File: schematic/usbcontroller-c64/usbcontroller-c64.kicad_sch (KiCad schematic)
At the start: 14 parts, among them J1 Conn_01x20_Socket, J2 Conn_01x20_Socket, J3 Conn_01x06_Socket, J4 Conn_01x02_Socket, Q1 PN2222A, Q2 PN2222A, Q3 PN2222A, Q4 PN2222A, Q5 PN2222A

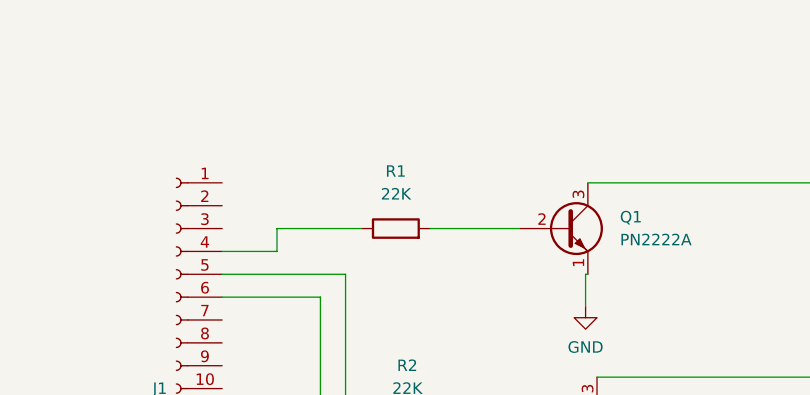
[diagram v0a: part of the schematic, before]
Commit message: add tx/rx for debug
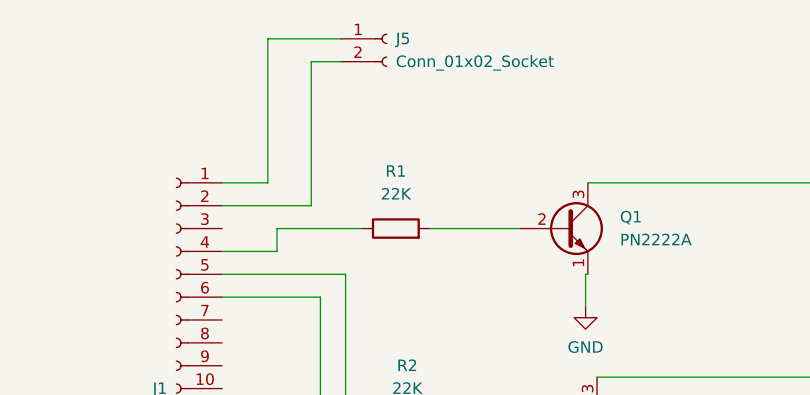
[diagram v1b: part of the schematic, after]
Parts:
- added J5: Conn_01x02_Socket, Connector_PinSocket_2.54mm:PinSocket_1x02_P2.54mm_Vertical, symbol Connector:Conn_01x02_Socket
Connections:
- net at J1.1 (Pin_1): now also J5.1 (Pin_1)
- net at J1.2 (Pin_2): now also J5.2 (Pin_2)
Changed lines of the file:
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@@
+    (stroke (width 0) (type default))
+  )
+  (wire (pts (xy 104.14 44.958) (xy 107.442 44.958))
     (stroke (width 0) (type default))
   )
@@
     (stroke (width 0) (type default))
   )
+  (wire (pts (xy 99.314 42.418) (xy 107.442 42.418))
+    (stroke (width 0) (type default))
+  )
   (wire (pts (xy 109.22 128.27) (xy 114.3 128.27))
     (stroke (width 0) (type default))
@@
     (stroke (width 0) (type default))
   )
+  (wire (pts (xy 99.314 58.42) (xy 99.314 42.418))
+    (stroke (width 0) (type default))
+  )
   (wire (pts (xy 67.564 122.936) (xy 109.22 122.936))
     (stroke (width 0) (type default))
   )
+  (wire (pts (xy 94.234 60.96) (xy 104.14 60.96))
+    (stroke (width 0) (type default))
+  )
   (wire (pts (xy 176.784 148.59) (xy 176.784 104.14))
     (stroke (width 0) (type default))
   )
+  (wire (pts (xy 94.234 58.42) (xy 99.314 58.42))
+    (stroke (width 0) (type default))
+  )
   (wire (pts (xy 138.176 132.334) (xy 138.176 137.414))
+    (stroke (width 0) (type default))
+  )
+  (wire (pts (xy 104.14 60.96) (xy 104.14 44.958))
     (stroke (width 0) (type default))
   )
@@
         )
       )
+    )
+  )
+  (symbol (lib_id "Connector:Conn_01x02_Socket") (at 112.522 42.418 0) (unit 1)
+    (in_bom yes) (on_board yes) (dnp no) (fields_autoplaced)
+    (property "Reference" "J5" (at 113.538 42.418 0)
+      (effects (font (size 1.27 1.27)) (justify left))
+    )
+    (property "Value" "Conn_01x02_Socket" (at 113.538 44.958 0)
+      (effects (font (size 1.27 1.27)) (justify left))
+    )
+    (property "Footprint" "Connector_PinSocket_2.54mm:PinSocket_1x02_P2.54mm_Vertical" (at 112.522 42.418 0)
+      (effects (font (size 1.27 1.27)) hide)
+    )
+    (property "Datasheet" "~" (at 112.522 42.418 0)
+      (effects (font (size 1.27 1.27)) hide)
+    )
+    (pin "1")
+    (pin "2")
+    (instances
+      (project "usbcontroller-c64"
+        (path "/8450b7a4-7acf-420a-93b2-b80915645b62"
+          (reference "J5") (unit 1)
+        )
+      )

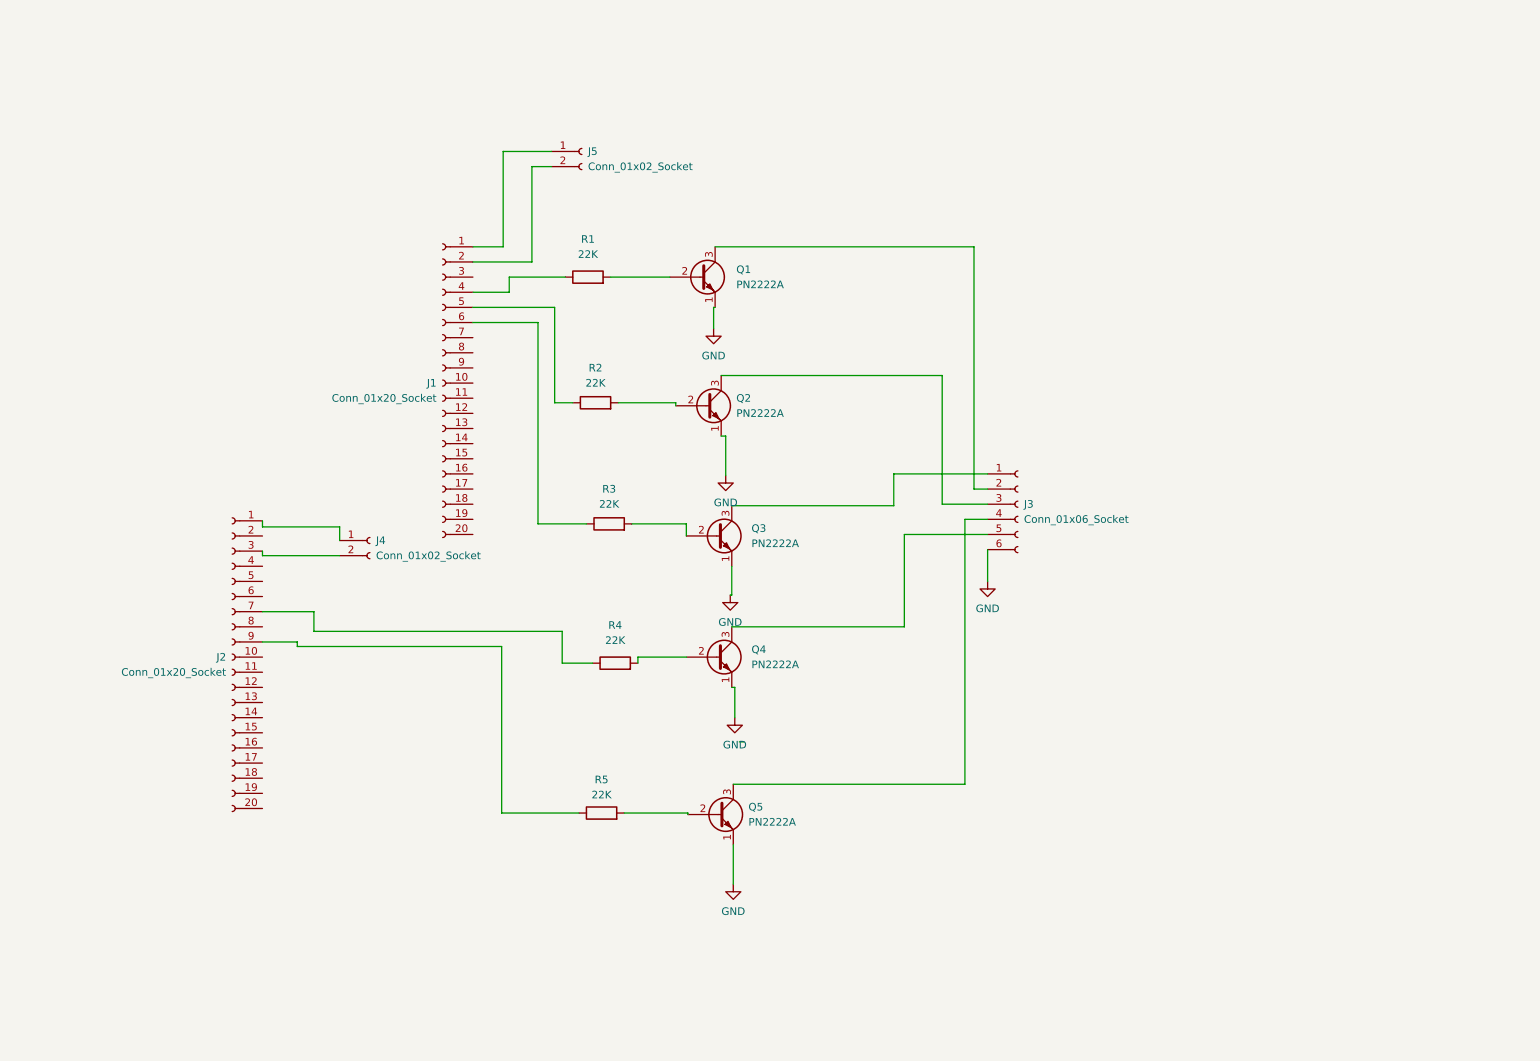
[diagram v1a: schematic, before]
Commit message: update schematic to usb db9 connector and power
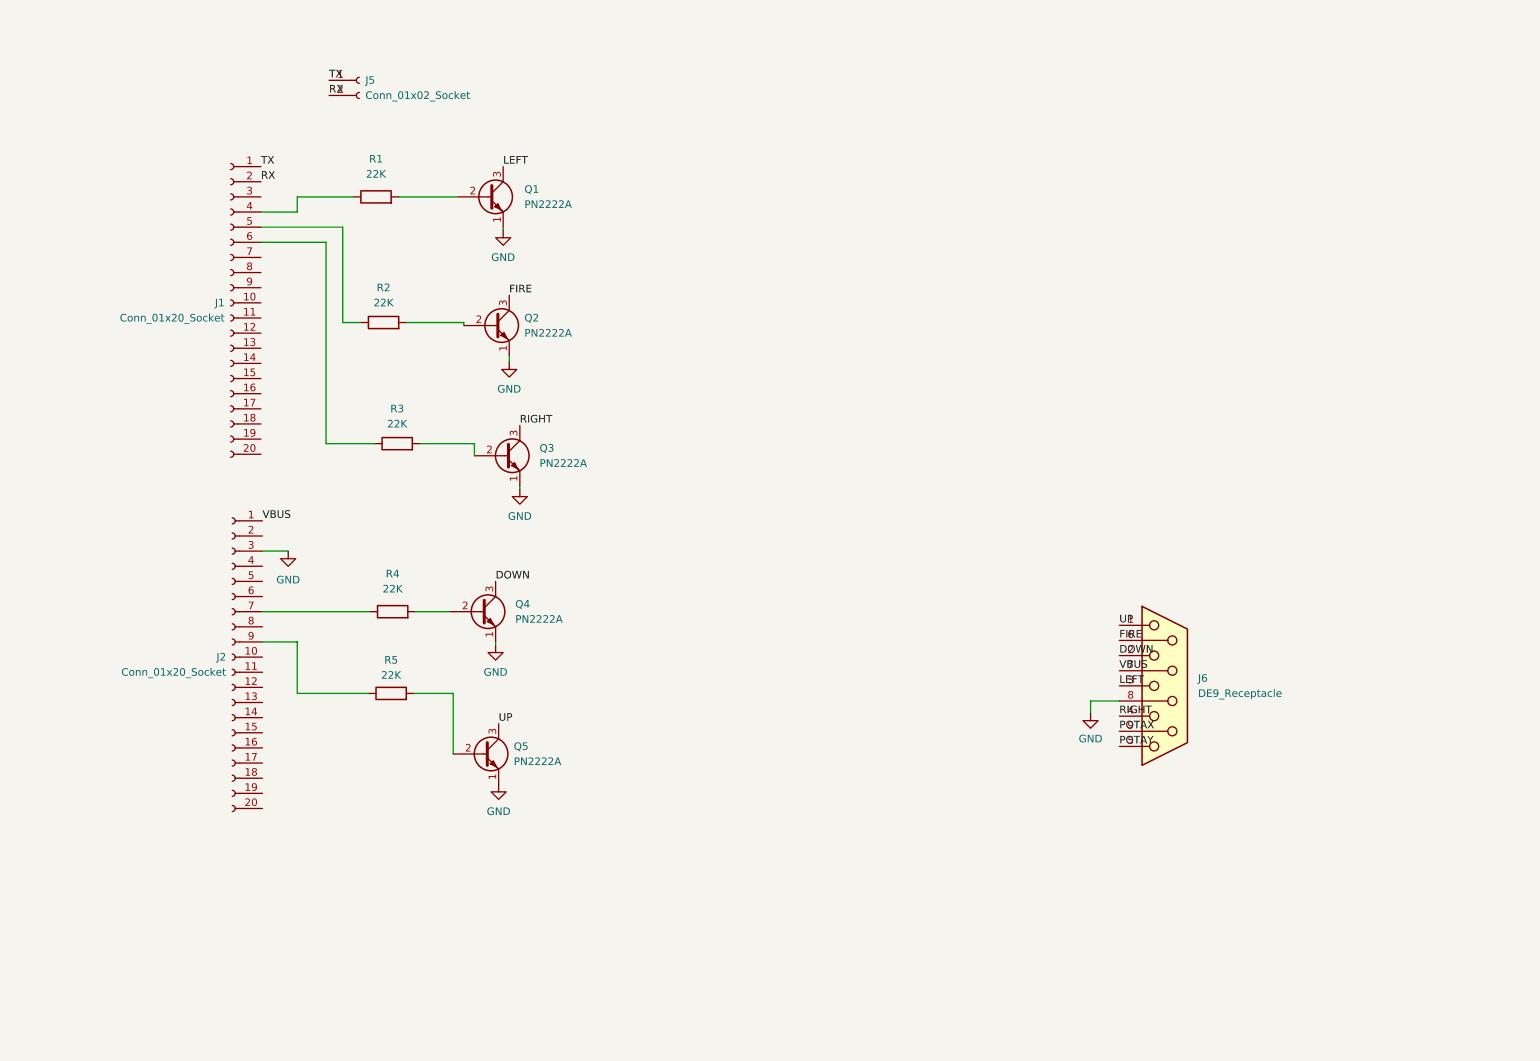
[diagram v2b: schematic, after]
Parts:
- removed J3: Conn_01x06_Socket, Connector_PinSocket_2.54mm:PinSocket_1x06_P2.54mm_Vertical, symbol Connector:Conn_01x06_Socket
- removed J4: Conn_01x02_Socket, Connector_PinSocket_2.54mm:PinSocket_1x02_P2.54mm_Vertical, symbol Connector:Conn_01x02_Socket
- added J6: DE9_Receptacle, Connector_Dsub:DSUB-9_Female_Horizontal_P2.77x2.84mm_EdgePinOffset7.70mm_Housed_MountingHolesOffset9.12mm, symbol Connector:DE9_Receptacle
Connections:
- net GND: now also J2.3 (Pin_3), J6.8
- net FIRE: now reaches Q2.3 (C)
- net FIRE: now also J6.6
- net UP: now reaches Q5.3 (C)
- net UP: now also J6.1
- net TX: now reaches J1.1 (Pin_1), J5.1 (Pin_1)
- net RX: now reaches J1.2 (Pin_2), J5.2 (Pin_2)
- net LEFT: now reaches Q1.3 (C)
- net LEFT: now also J6.3
- net RIGHT: now reaches Q3.3 (C)
- net RIGHT: now also J6.4
- net DOWN: now reaches Q4.3 (C)
- net DOWN: now also J6.2
- net VBUS: now reaches J2.1 (Pin_1)
- net VBUS: now also J6.7
- new net POTAX: J6.9
- new net POTAY: J6.5
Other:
- moved on the sheet: J1, J5, Q1, Q2, Q3, Q4, Q5, R1, R2, R3, R4, R5

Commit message: remove forked pico-sdk depeancy and get back on the normal one
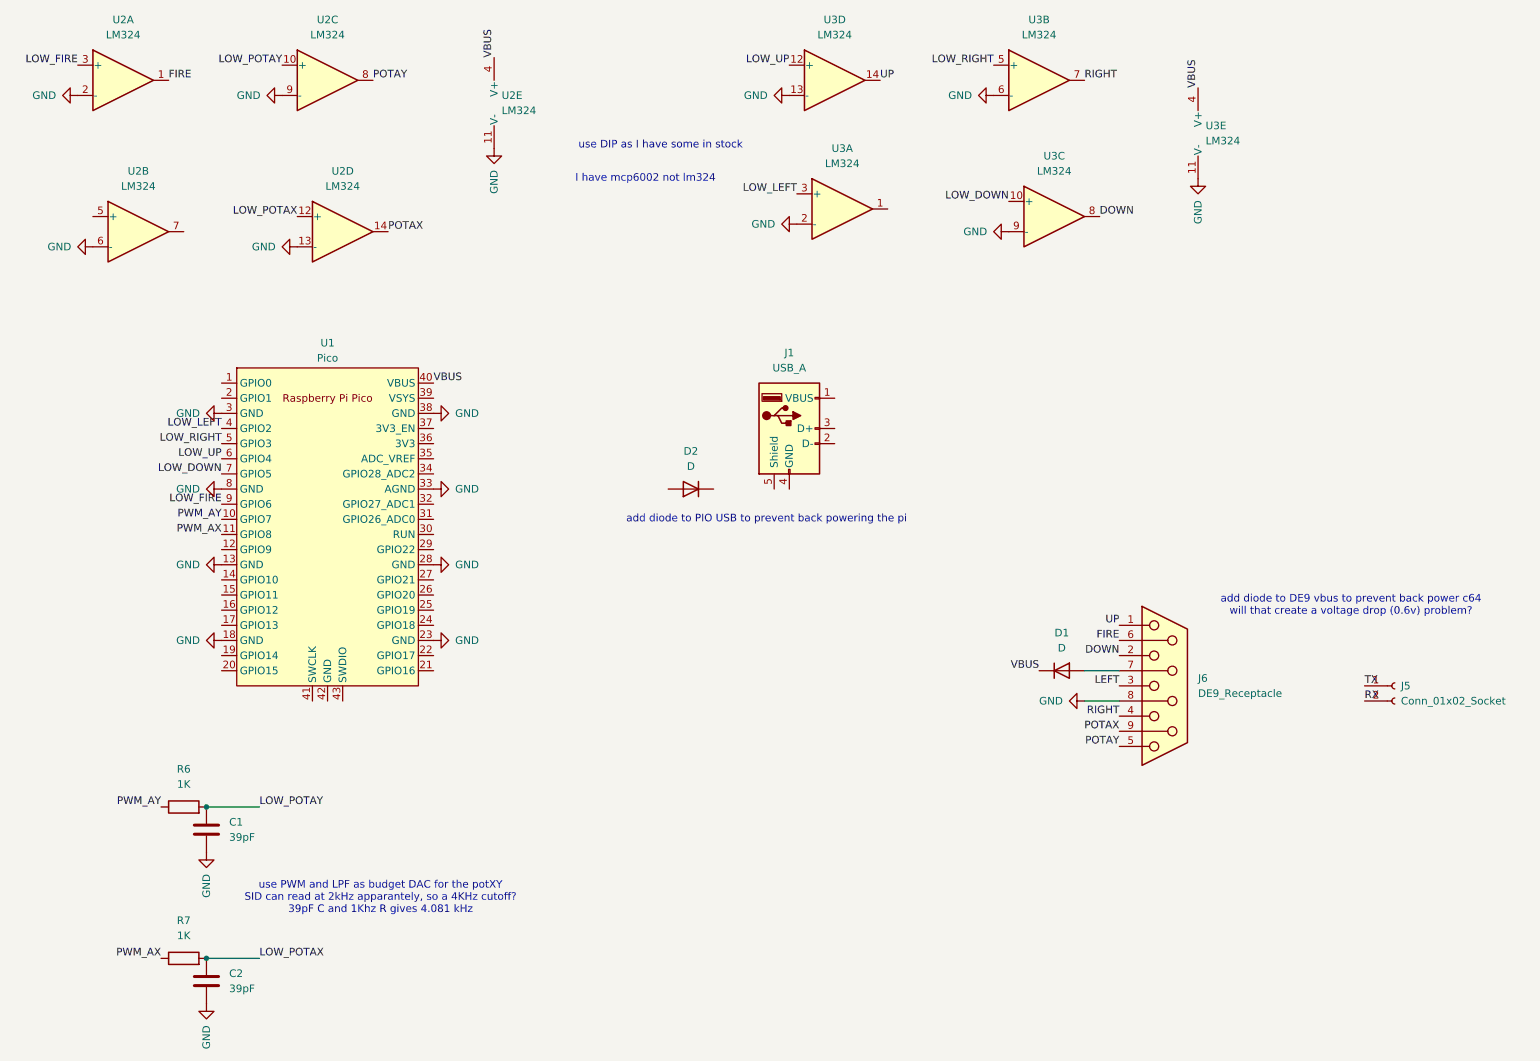
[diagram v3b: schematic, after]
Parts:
- removed J1, J2: Conn_01x20_Socket, Connector_PinSocket_2.54mm:PinSocket_1x20_P2.54mm_Vertical, symbol Connector:Conn_01x20_Socket
- removed Q1, Q2, Q3, Q4, Q5: PN2222A, Package_TO_SOT_THT:TO-92_Inline, symbol Transistor_BJT:PN2222A
- removed R1, R2, R3, R4, R5: 22K, Resistor_THT:R_Axial_DIN0207_L6.3mm_D2.5mm_P10.16mm_Horizontal, symbol Device:R
- added C1, C2: 39pF, Capacitor_THT:CP_Radial_D5.0mm_P2.50mm, symbol Device:C
- added D1, D2: D, symbol Device:D
- added J1: USB_A, symbol Connector:USB_A
- added R6, R7: 1K, Resistor_THT:R_Axial_DIN0207_L6.3mm_D2.5mm_P10.16mm_Horizontal, symbol Device:R
- added U1: Pico, RPi_Pico:RPi_Pico_SMD_TH, symbol MCU_RaspberryPi_and_Boards:Pico
- added U2, U3: LM324, symbol Amplifier_Operational:LM324
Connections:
- net DOWN: now also U3.8
- net FIRE: now also U2.1
- net GND: now also C1.2, C2.2, U1.13 (GND), U1.18 (GND), U1.23 (GND), U1.28 (GND), U1.3 (GND), U1.33 (AGND), U1.38 (GND), U1.8 (GND), U2.11 (V-), U2.13 (-), U2.2 (-), U2.6 (-), U2.9 (-), U3.11 (V-), U3.13 (-), U3.2 (-), U3.6 (-), U3.9 (-)
- net POTAX: now also U2.14
- net POTAY: now also U2.8
- net RIGHT: now also U3.7
- net UP: now also U3.14
- net VBUS: now also D1.1 (K), U1.40 (VBUS), U2.4 (V+), U3.4 (V+); no longer J6.7
- new net: D1.2 (A), J6.7
- new net LOW_DOWN: U1.7 (GPIO5), U3.10 (+)
- new net LOW_FIRE: U1.9 (GPIO6), U2.3 (+)
- new net LOW_LEFT: U1.4 (GPIO2), U3.3 (+)
- new net LOW_POTAX: C2.1, R7.2, U2.12 (+)
- new net LOW_POTAY: C1.1, R6.2, U2.10 (+)
- new net LOW_RIGHT: U1.5 (GPIO3), U3.5 (+)
- new net LOW_UP: U1.6 (GPIO4), U3.12 (+)
- new net PWM_AX: R7.1, U1.11 (GPIO8)
- new net PWM_AY: R6.1, U1.10 (GPIO7)
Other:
- note added: "I have mcp6002 not lm324"
- note added: "add diode to DE9 vbus to prevent back power c64 will that create a voltage drop (0.6v) problem?"
- note added: "add diode to PIO USB to prevent back powering the pi"
- note added: "use DIP as I have some in stock"
- note added: "use PWM and LPF as budget DAC for the potXY SID can read at 2kHz apparantely, so a 4KHz cutoff? 39pF C and 1Khz R gives 4.081 kHz"
- moved on the sheet: J5
